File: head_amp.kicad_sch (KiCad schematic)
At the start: 26 parts, among them J1 Conn_01x02, J2 Headset Port, J3 Ear Mic Input, J4 Speaker Output, SW1 SW_Wuerth_450301014042, U1 LM124DR

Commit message: Route PCB :3
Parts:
- removed R11, R12, R3, R4: 10k, Resistor_SMD:R_1206_3216Metric_Pad1.30x1.75mm_HandSolder, symbol Device:R
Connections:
- net VRef: now reaches U1.10 (+)
- net VRef: now also R6.1, R8.1, U1.3 (+), U1.5 (+)
- net at R9.2, RV2.2, U1.9 (-): no longer RV2.3
- net at U1.12 (+): now also U1.13 (-)
- no-connect marks 6 -> 5
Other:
- moved on the sheet: R6, R8

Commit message: Delete schematic and PCB
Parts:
- removed C1, C3, C5: 0.1u, Capacitor_SMD:C_1206_3216Metric_Pad1.33x1.80mm_HandSolder, symbol Device:C
- removed C2, C4, C6: 4.7u, Capacitor_SMD:C_1206_3216Metric_Pad1.33x1.80mm_HandSolder, symbol Device:C
- removed J1: Conn_01x02, Connector_Wire:SolderWire-0.1sqmm_1x02_P3.6mm_D0.4mm_OD1mm, symbol Connector_Generic:Conn_01x02
- removed J2: Headset Port, Connector_Audio:Jack_3.5mm_PJ320E_Horizontal, symbol Connector_Audio:AudioJack3_Ground
- removed J3: Ear Mic Input, Connector_Audio:Jack_3.5mm_Lumberg_1503_07_Horizontal, symbol Connector_Audio:AudioJack2_Ground
- removed J4: Speaker Output, Connector_Audio:Jack_3.5mm_Lumberg_1503_07_Horizontal, symbol Connector_Audio:AudioJack2_Ground
- removed R1, R10, R5, R6, R8: 10k, Resistor_SMD:R_1206_3216Metric_Pad1.30x1.75mm_HandSolder, symbol Device:R
- removed R2, R7, R9: 1k, Resistor_SMD:R_1206_3216Metric_Pad1.30x1.75mm_HandSolder, symbol Device:R
- removed RV1: R_Potentiometer_Dual_Separate, Potentiometer_THT:Potentiometer_Piher_T-16H_Double_Horizontal, symbol Device:R_Potentiometer_Dual_Separate
- removed RV2: R_Potentiometer, Potentiometer_THT:Potentiometer_ACP_CA6-H2,5_Horizontal, symbol Device:R_Potentiometer
- removed SW1: SW_Wuerth_450301014042, Button_Switch_THT:SW_Slide-03_Wuerth-WS-SLTV_10x2.5x6.4_P2.54mm, symbol Switch:SW_Wuerth_450301014042
- removed U1: LM124DR, LM124DR:SOIC127P600X175-14N, symbol Amplifier_Operational:OPA1679
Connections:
- no-connect marks 5 -> 0

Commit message: Lots of stuff
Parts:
- added C1, C10, C13, C15, C17, C18, C19, C2, C4, C5, C7, C9: 100n, Capacitor_SMD:C_0603_1608Metric, symbol Device:C
- added C11, C12, C16, C3, C6: 1u, Capacitor_SMD:C_0603_1608Metric, symbol Device:C
- added C14, C8: 2.2u, Capacitor_SMD:C_0603_1608Metric, symbol Device:C
- added D1: RX_LED, LED_SMD:LED_0603_1608Metric, symbol Device:LED
- added D2: TX_LED, LED_SMD:LED_0603_1608Metric, symbol Device:LED
- added J1: USB Interface, Connector_USB:USB_C_Receptacle_GCT_USB4105-xx-A_16P_TopMnt_Horizontal, symbol Connector:USB_C_Receptacle_USB2.0_16P
- added J3: AudioJack4, Connector_Audio:Jack_3.5mm_PJ320D_Horizontal, symbol Connector_Audio:AudioJack4
- added M1: Fan, A2543WR-4P:MOLEX_22053041, symbol Motor:Fan_Tacho_PWM
- added Q1: AO3401A, Package_TO_SOT_SMD:SOT-23, symbol Transistor_FET:AO3401A
- added Q2: BSS138, Package_TO_SOT_SMD:SOT-23, symbol Transistor_FET:BSS138
- added Q3, Q4: LRC L8050QLT1G, Package_TO_SOT_SMD:SOT-23, symbol Transistor_BJT:Q_NPN_BEC
- added R1, R3, R4: 10k, Resistor_SMD:R_0603_1608Metric, symbol Device:R
- added R10, R9: 1k, Resistor_SMD:R_0603_1608Metric, symbol Device:R
- added R2, R7, R8: 5.1k, Resistor_SMD:R_0603_1608Metric, symbol Device:R
- added R5, R6: 22, Resistor_SMD:R_0603_1608Metric, symbol Device:R
- added TP1: Boot, TestPoint:TestPoint_2Pads_Pitch5.08mm_Drill1.3mm, symbol Connector:TestPoint_2Pole
- added TP2: Reset, TestPoint:TestPoint_2Pads_Pitch5.08mm_Drill1.3mm, symbol Connector:TestPoint_2Pole
- added U1, U5: TXS0102DCU, Package_SO:VSSOP-8_2.3x2mm_P0.5mm, symbol Logic_LevelTranslator:TXS0102DCU
- added U2: CH340K, Package_SO:SSOP-10-1EP_3.9x4.9mm_P1mm_EP2.1x3.3mm, symbol Interface_USB:CH340K
- added U3: Digital Regulator, Package_TO_SOT_SMD:TO-252-2, symbol Regulator_Linear:LT1084-3.3
- added U4: Analog Regulator, Package_TO_SOT_SMD:TO-252-2, symbol Regulator_Linear:LT1084-3.3
- added U6: ESP32-S3-WROOM-1, RF_Module:ESP32-S3-WROOM-1, symbol RF_Module:ESP32-S3-WROOM-1
- added U7: LSM6DS3, Package_LGA:LGA-14_3x2.5mm_P0.5mm_LayoutBorder3x4y, symbol Sensor_Motion:LSM6DS3
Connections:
- new net: J1.A6 (D+), J1.B6 (D+), R6.1
- new net: D1.1 (K), R9.2
- new net: Q3.1 (B), R3.2
- new net: J1.A7 (D-), J1.B7 (D-), R5.1
- new net: M1.4 (PWM), U5.1 (B2)
- new net: M1.3 (Tacho), U5.8 (B1)
- new net: Q4.1 (B), R4.2
- new net: Q1.3 (D), Q2.3 (D)
- new net: C5.1, U2.10 (V3)
- new net: J1.B5 (CC2), R8.1
- new net: J1.A5 (CC1), R7.1
- new net: D2.1 (K), R10.2
- new net +3V3A: C14.1, U4.2 (VO)
- new net +3V3D: C1.2, C10.2, C12.2, C13.2, C18.1, C19.1, C4.2, C8.1, D1.2 (A), D2.2 (A), U1.3 (VCCA), U1.6 (OE), U2.7 (VCC), U3.2 (VO), U5.3 (VCCA), U5.6 (OE), U6.2 (3V3), U7.5 (VDDIO), U7.8 (VDD)
- new net DTR: Q4.2 (E), R3.1, U2.4 (~{DTR})
- new net FAN_PWM: Q1.1 (G), Q2.1 (G), U1.4 (A2), U5.4 (A2)
- new net FAN_RPM: R1.1, R2.2, U1.5 (A1), U5.5 (A1)
- new net GND: C1.1, C10.1, C11.2, C12.1, C13.1, C14.2, C15.1, C16.1, C17.2, C18.2, C19.2, C2.1, C3.1, C4.1, C5.2, C6.2, C7.2, C8.2, C9.2, J1.A1 (GND), J1.A12 (GND), J1.B1 (GND), J1.B12 (GND), J1.S1 (SHIELD), J3.R2, M1.1 (-), Q2.2 (S), R1.2, R7.2, R8.2, TP1.2, TP2.2, U1.2 (GND), U2.11 (GND), U2.3 (GND), U3.1 (GND), U4.1 (GND), U5.2 (GND), U6.1 (GND), U6.40 (GND), U6.41 (GND), U7.6 (GND), U7.7 (GND)
- new net GPIO0: C7.1, Q4.3 (C), TP1.1, U6.27 (IO0)
- new net Headset_Left: J3.T
- new net Headset_Mic: J3.S
- new net Headset_Right: J3.R1
- new net IMU_Select: U7.12 (CS)
- new net MCU_EN: C9.1, Q3.3 (C), TP2.1, U6.3 (EN)
- new net MCU_RX: R9.1, U2.8 (TXD), U6.36 (RXD0)
- new net MCU_TX: R10.1, U2.9 (RXD), U6.37 (TXD0)
- new net MISO: U7.1 (SDO/SA0)
- new net MOSI: U7.14 (SDA)
- new net RTS: Q3.2 (E), R4.1, U2.6 (~{RTS})
- new net SPI_CLK: U7.13 (SCL)
- new net USB_D+: R6.2, U2.1 (UD+)
- new net USB_D-: R5.2, U2.2 (UD-)
- new net VBUS: C11.1, C15.2, C16.2, C17.1, C2.2, C3.2, C6.1, J1.A4 (VBUS), J1.A9 (VBUS), J1.B4 (VBUS), J1.B9 (VBUS), M1.2 (+), Q1.2 (S), U1.7 (VCCB), U3.3 (VI), U4.3 (VI), U5.7 (VCCB)
- no-connect marks 0 -> 7
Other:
- added sheet Ext->Int (codec.kicad_sch)
- added sheet Int->Ext (codec.kicad_sch)
- note added: "TODO: Add Capacitors Here"

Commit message: More stuff
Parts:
- removed C1, C2: 100n, Capacitor_SMD:C_0603_1608Metric, symbol Device:C
- removed C3: 1u, Capacitor_SMD:C_0603_1608Metric, symbol Device:C
- removed Q1: AO3401A, Package_TO_SOT_SMD:SOT-23, symbol Transistor_FET:AO3401A
- removed Q2: BSS138, Package_TO_SOT_SMD:SOT-23, symbol Transistor_FET:BSS138
- removed R1: 10k, Resistor_SMD:R_0603_1608Metric, symbol Device:R
- removed R2: 5.1k, Resistor_SMD:R_0603_1608Metric, symbol Device:R
- removed TP1: Boot, TestPoint:TestPoint_2Pads_Pitch5.08mm_Drill1.3mm, symbol Connector:TestPoint_2Pole
- removed TP2: Reset, TestPoint:TestPoint_2Pads_Pitch5.08mm_Drill1.3mm, symbol Connector:TestPoint_2Pole
- removed U1: TXS0102DCU, Package_SO:VSSOP-8_2.3x2mm_P0.5mm, symbol Logic_LevelTranslator:TXS0102DCU
- added C17, C18: 220u, Capacitor_SMD:CP_Elec_5x5.4, symbol Device:C_Polarized
- added J2: Left_Mic, Connector_JST:JST_XH_S2B-XH-A_1x02_P2.50mm_Horizontal, symbol Connector_Generic:Conn_01x02
- added J3: Right_Mic, Connector_JST:JST_XH_S2B-XH-A_1x02_P2.50mm_Horizontal, symbol Connector_Generic:Conn_01x02
- added R10, R11: 10k, Resistor_SMD:R_0603_1608Metric, symbol Device:R
- added R9: 0, Resistor_SMD:R_2512_6332Metric, symbol Device:R
- added SW1: Boot, Button_Switch_THT:SW_Tactile_SPST_Angled_PTS645Vx39-2LFS, symbol Switch:SW_Push
- added SW2: Reset, Button_Switch_THT:SW_Tactile_SPST_Angled_PTS645Vx39-2LFS, symbol Switch:SW_Push
- C1: renamed from C4; LCSC C48579280 -> (none)
- C10: renamed from C13; LCSC C48579280 -> (none)
- C12: renamed from C15; LCSC C48579280 -> (none)
- C13: renamed from C16; LCSC C48579280 -> (none)
- C14: renamed from C17; LCSC C48579280 -> (none)
- C15: renamed from C18; LCSC C48579280 -> (none)
- C16: renamed from C19; LCSC C48579280 -> (none)
- C2: renamed from C5; LCSC C48579280 -> (none)
- C4: renamed from C7; LCSC C48579280 -> (none)
- C6: renamed from C9; LCSC C48579280 -> (none)
- C7: renamed from C10; LCSC C48579280 -> (none)
- C9: renamed from C12; LCSC C6119849 -> (none)
- R1: renamed from R3; LCSC C2930027 -> (none)
- R2: renamed from R4; LCSC C2930027 -> (none)
- R7: renamed from R9; LCSC C2907113 -> (none)
- R8: renamed from R10; LCSC C2907113 -> (none)
- U6: renamed from U7; LCSC (none) -> C95230
- renumbered C14 to C11, C6 to C3, C8 to C5, C11 to C8, J3 to J4, Q3 to Q1, Q4 to Q2, R5 to R3, R6 to R4, R7 to R5, R8 to R6, U2 to U1, U3 to U2, U4 to U3, U5 to U4, U6 to U5
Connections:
- net GND: now also U6.2 (SDX), U6.3 (SCX), R9.1, SW1.1, SW2.1; no longer C11.2, C8.2, J4.R2, U3.1 (GND)
- net GPIO0: now also SW1.2
- net Headset_Left: now also C18.2
- net Headset_Right: now also C17.2
- net MCU_EN: now also SW2.2
- new net Ext->Int/OUT_Left: C18.1
- new net Ext->Int/OUT_Right: C17.1
- new net GNDA: C11.2, C8.2, J2.2 (Pin_2), J3.2 (Pin_2), J4.R2, R9.2, U3.1 (GND)
- new net Mic_Left: J2.1 (Pin_1), R10.1
- new net Mic_Right: J3.1 (Pin_1), R11.1
- new net VDD: R10.2, R11.2
- no-connect marks 7 -> 5
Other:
- note removed: "TODO: Add Capacitors Here"
- moved on the sheet: J4

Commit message: Fixes
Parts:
- removed C17, C18: 220u, Capacitor_SMD:CP_Elec_5x5.4, symbol Device:C_Polarized
- added J2: Left_Speaker, Connector_JST:JST_XH_S2B-XH-A_1x02_P2.50mm_Horizontal, symbol Connector_Generic:Conn_01x02
- added J4: Right_Speaker, Connector_JST:JST_XH_S2B-XH-A_1x02_P2.50mm_Horizontal, symbol Connector_Generic:Conn_01x02
- added R12: 10k, Resistor_SMD:R_0603_1608Metric, symbol Device:R
- renumbered J2 to J3, J3 to J5, J4 to J6
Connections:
- net GNDA: now also J2.2 (Pin_2), J4.2 (Pin_2)
- net Headset_Mic: now also R12.1
- net VDD: now also R12.2
- new net Speaker_Left: J2.1 (Pin_1)
- new net Speaker_Right: J4.1 (Pin_1)
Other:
- moved on the sheet: J3, J5, J6, R10, R11

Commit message: started compact layout
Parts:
- removed D1: RX_LED, LED_SMD:LED_0603_1608Metric, symbol Device:LED
- removed D2: TX_LED, LED_SMD:LED_0603_1608Metric, symbol Device:LED
- removed R7, R8: 1k, Resistor_SMD:R_0603_1608Metric, symbol Device:R
- removed R9: 0, Resistor_SMD:R_2512_6332Metric, symbol Device:R
- added NT1: NetTie_2, symbol Device:NetTie_2
- C11, C5: value 2.2u -> 22u
- C3, C8: value 1u -> 10u
- renumbered R5 to R3, R6 to R4, R3 to R5, R4 to R6, R10 to R7, R11 to R8, R12 to R9
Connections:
- net VDD is gone; now on net +3V3A: R7.2, R8.2, R9.2
- net FAN_PWM: now also U5.4 (IO4)
- net FAN_RPM: now also U5.5 (IO5)
- net GND: now also NT1.1
- net GNDA: now also NT1.2
- net USB_D1+: now reaches J1.A6 (D+), J1.B6 (D+), R6.1
- net USB_D1-: now reaches J1.A7 (D-), J1.B7 (D-), R5.1
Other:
- moved on the sheet: R5, R6

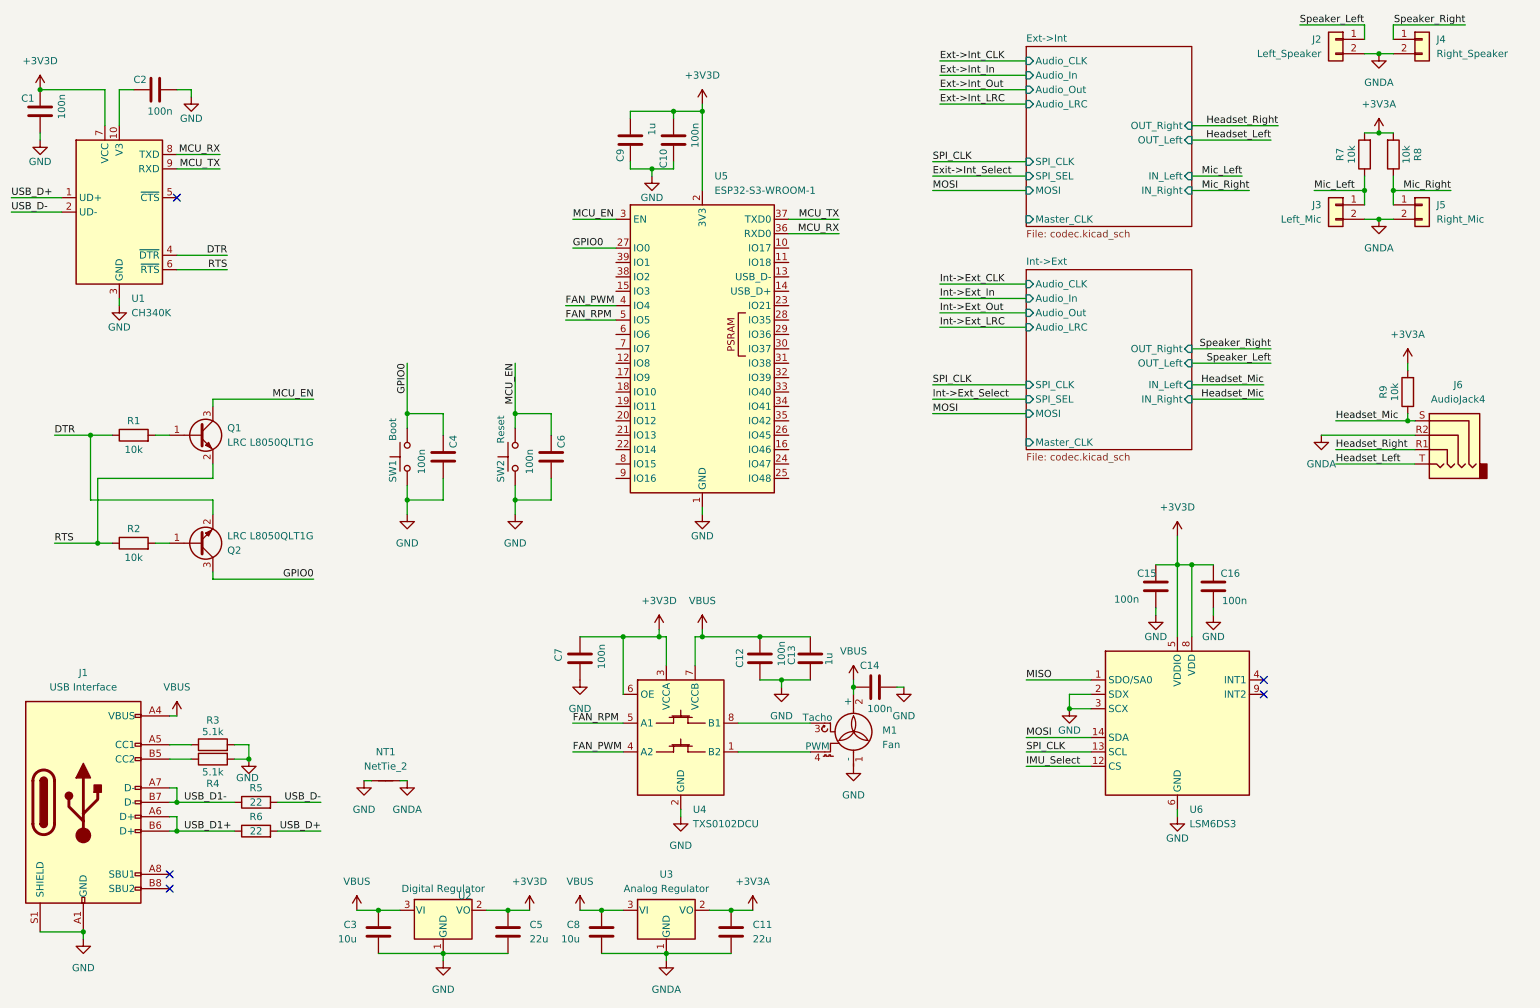
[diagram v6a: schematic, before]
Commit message: feat: start hat version
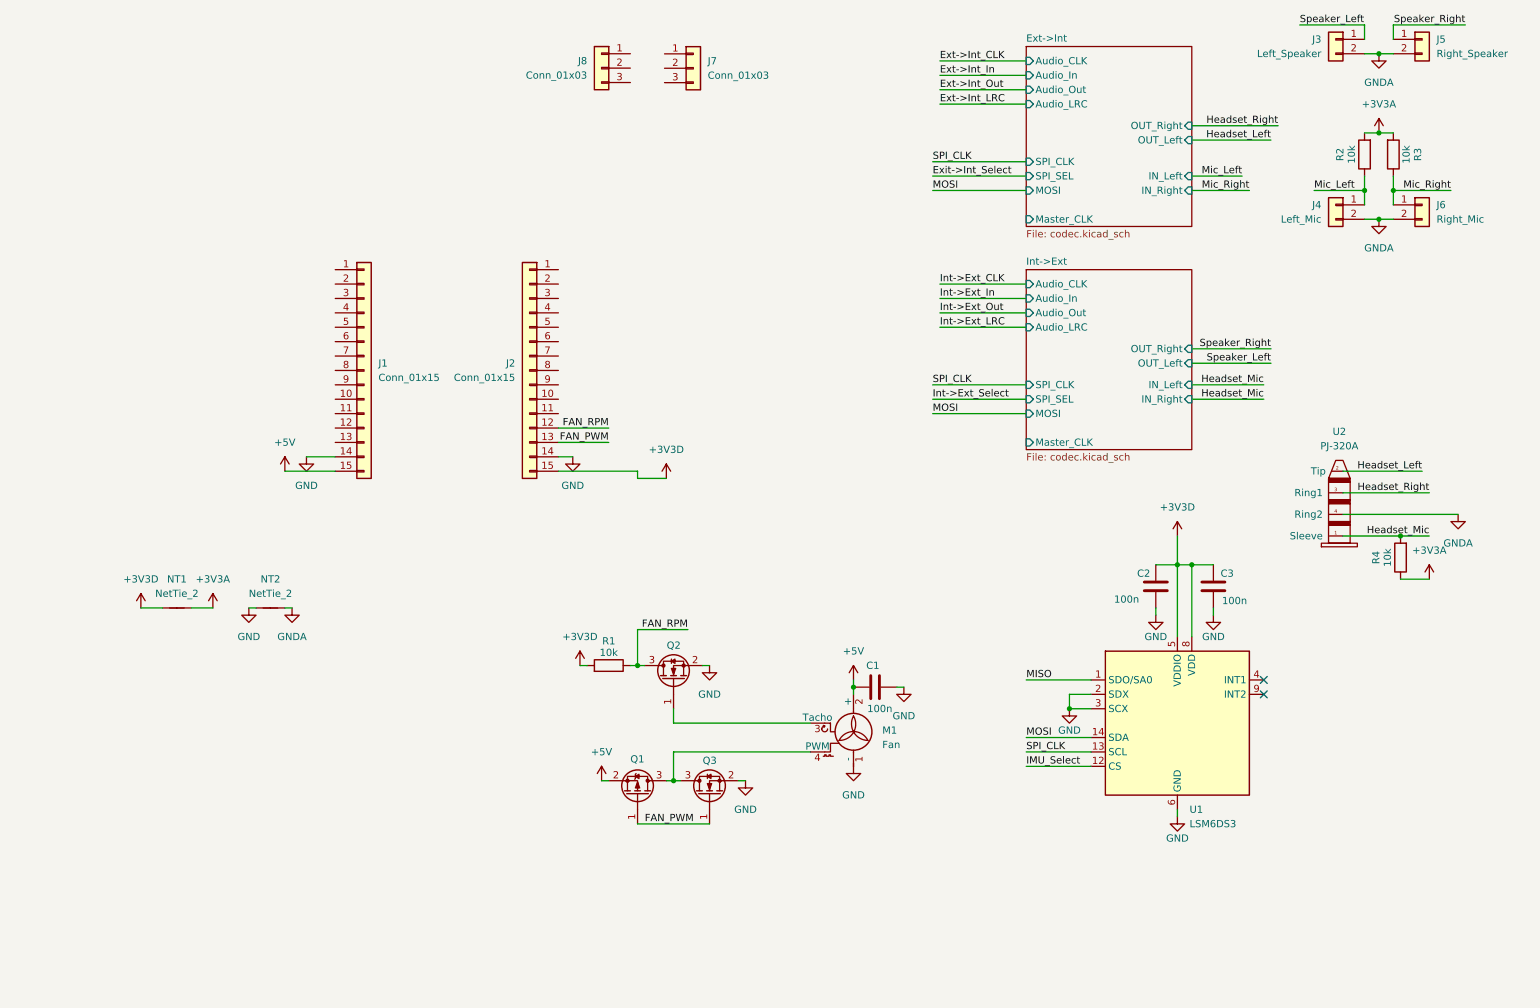
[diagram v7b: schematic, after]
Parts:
- removed C1, C10, C12, C2, C4, C6, C7: 100n, Capacitor_SMD:C_0603_1608Metric, symbol Device:C
- removed C11, C5: 22u, Capacitor_SMD:C_0603_1608Metric, symbol Device:C
- removed C13, C9: 1u, Capacitor_SMD:C_0603_1608Metric, symbol Device:C
- removed C3, C8: 10u, Capacitor_SMD:C_0603_1608Metric, symbol Device:C
- removed J1: USB Interface, Connector_USB:USB_C_Receptacle_GCT_USB4105-xx-A_16P_TopMnt_Horizontal, symbol Connector:USB_C_Receptacle_USB2.0_16P
- removed J6: AudioJack4, Connector_Audio:Jack_3.5mm_PJ320D_Horizontal, symbol Connector_Audio:AudioJack4
- removed Q1, Q2: LRC L8050QLT1G, Package_TO_SOT_SMD:SOT-23, symbol Transistor_BJT:Q_NPN_BEC
- removed R2, R9: 10k, Resistor_SMD:R_0603_1608Metric, symbol Device:R
- removed R3: 5.1k, Resistor_SMD:R_0603_1608Metric, symbol Device:R
- removed R5, R6: 22, Resistor_SMD:R_0603_1608Metric, symbol Device:R
- removed SW1: Boot, Button_Switch_THT:SW_Tactile_SPST_Angled_PTS645Vx39-2LFS, symbol Switch:SW_Push
- removed SW2: Reset, Button_Switch_THT:SW_Tactile_SPST_Angled_PTS645Vx39-2LFS, symbol Switch:SW_Push
- removed U1: CH340K, Package_SO:SSOP-10-1EP_3.9x4.9mm_P1mm_EP2.1x3.3mm, symbol Interface_USB:CH340K
- removed U2: Digital Regulator, Package_TO_SOT_SMD:TO-252-2, symbol Regulator_Linear:LT1084-3.3
- removed U3: Analog Regulator, Package_TO_SOT_SMD:TO-252-2, symbol Regulator_Linear:LT1084-3.3
- removed U4: TXS0102DCU, Package_SO:VSSOP-8_2.3x2mm_P0.5mm, symbol Logic_LevelTranslator:TXS0102DCU
- removed U5: ESP32-S3-WROOM-1, RF_Module:ESP32-S3-WROOM-1, symbol RF_Module:ESP32-S3-WROOM-1
- added J1, J2: Conn_01x15, Connector_PinHeader_2.54mm:PinHeader_1x15_P2.54mm_Vertical, symbol Connector_Generic:Conn_01x15
- added J7, J8: Conn_01x03, Connector_JST:JST_XH_S3B-XH-A_1x03_P2.50mm_Horizontal, symbol Connector_Generic:Conn_01x03
- added NT1: NetTie_2, symbol Device:NetTie_2
- added Q1: AO3401A, Package_TO_SOT_SMD:SOT-23, symbol Transistor_FET:AO3401A
- added Q2, Q3: AO3400A, Package_TO_SOT_SMD:SOT-23, symbol Transistor_FET:AO3400A
- added U2: PJ-320A, PJ-320A:PJ-320A, symbol PJ-320A_Library:PJ-320A
- R4: value 5.1k -> 10k
- renumbered C14 to C1, C15 to C2, C16 to C3, J2 to J3, J3 to J4, J4 to J5, J5 to J6, NT1 to NT2, R7 to R2, R8 to R3, U6 to U1
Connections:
- net DTR is gone; now on net FAN_RPM: R1.1
- net +3V3A: now also R4.1, NT1.2
- net +3V3D: now also R1.2, J2.15 (Pin_15), NT1.1
- net FAN_PWM: now also J2.13 (Pin_13), Q1.1 (G), Q3.1 (G)
- net FAN_RPM: now also J2.12 (Pin_12), Q2.3 (D)
- net GND: now also J1.14 (Pin_14), J2.14 (Pin_14), Q2.2 (S), Q3.2 (S); no longer R4.2
- net GNDA: now also U2.4 (Ring2)
- net Headset_Left: now also U2.2 (Tip)
- net Headset_Mic: now also R4.2, U2.1 (Sleeve)
- net Headset_Right: now also U2.3 (Ring1)
- net at M1.4 (PWM): now also Q1.3 (D), Q3.3 (D)
- net at M1.3 (Tacho): now also Q2.1 (G)
- net VBUS renamed +5V
- net +5V: now also J1.15 (Pin_15), Q1.2 (S)
- no-connect marks 5 -> 2
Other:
- moved on the sheet: NT2
